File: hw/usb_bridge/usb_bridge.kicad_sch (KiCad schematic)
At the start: 57 parts, among them J1 USB_C_Receptacle_USB2.0_14P, J2 DE9, U1 CH340E, U2 MAX485E, U3 CH334R, U4 74LVC2G04, U5 MCP1754S-3302xCB, U6 TJA1051T-3, Y1 HCI XC53G2-12.000-F20LJDT

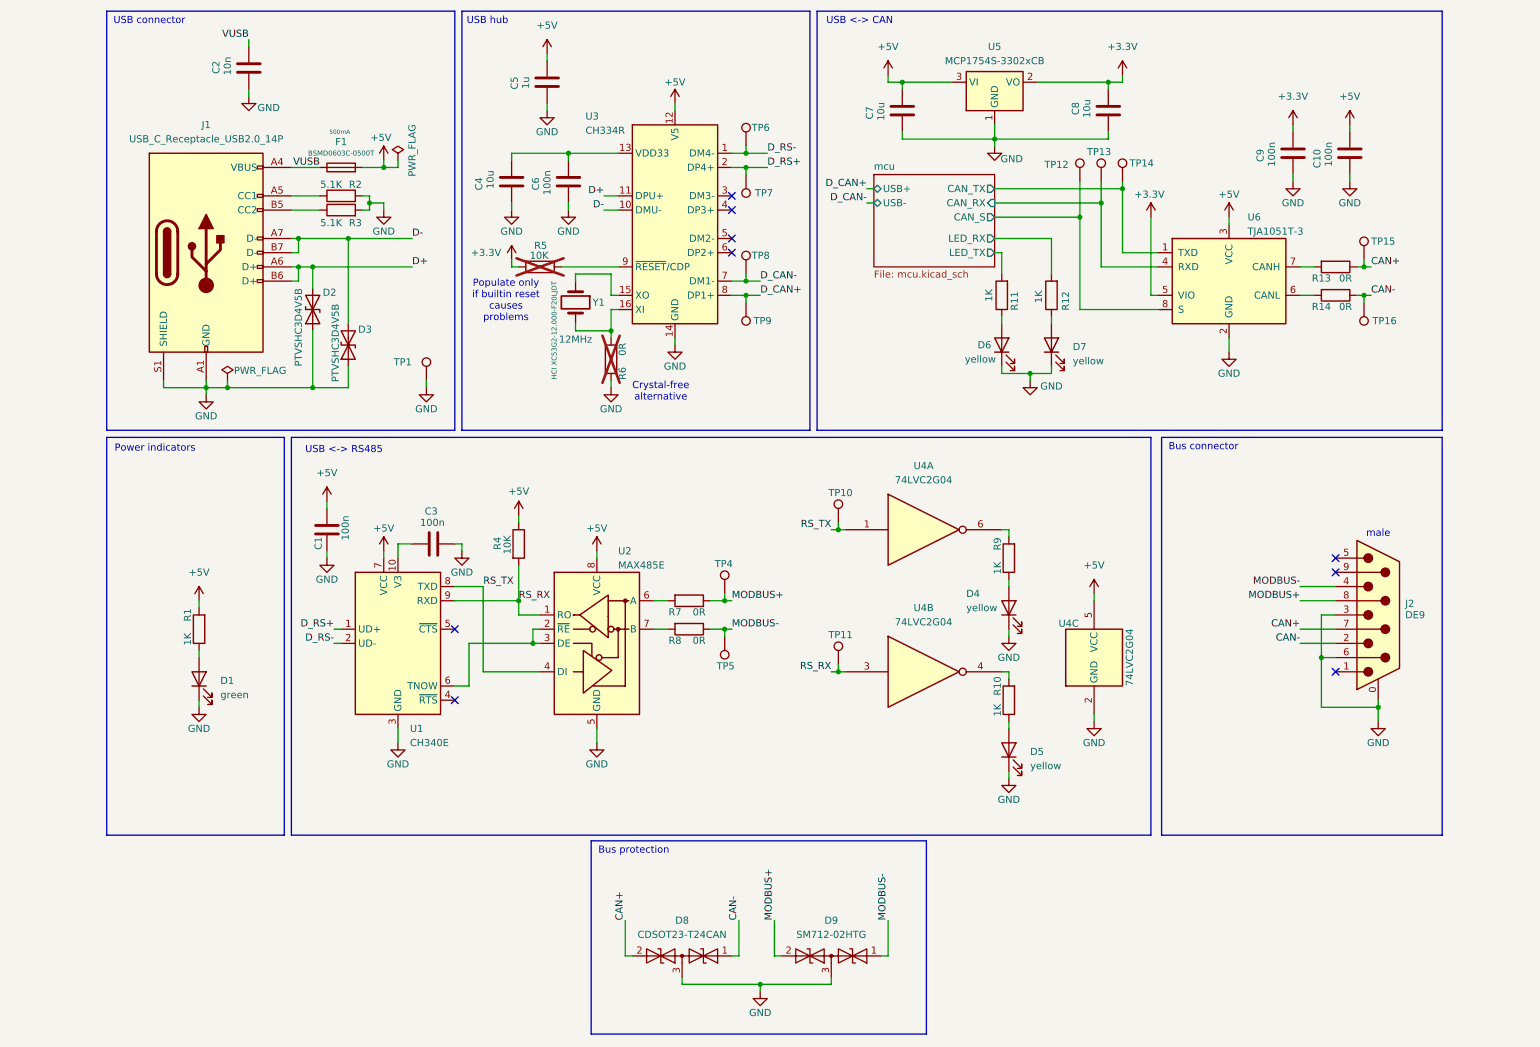
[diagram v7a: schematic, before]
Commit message: Add LED jumper
Signed-off-by: Mateusz Pająk <22417805+Tai-Min@users.noreply.github.com>
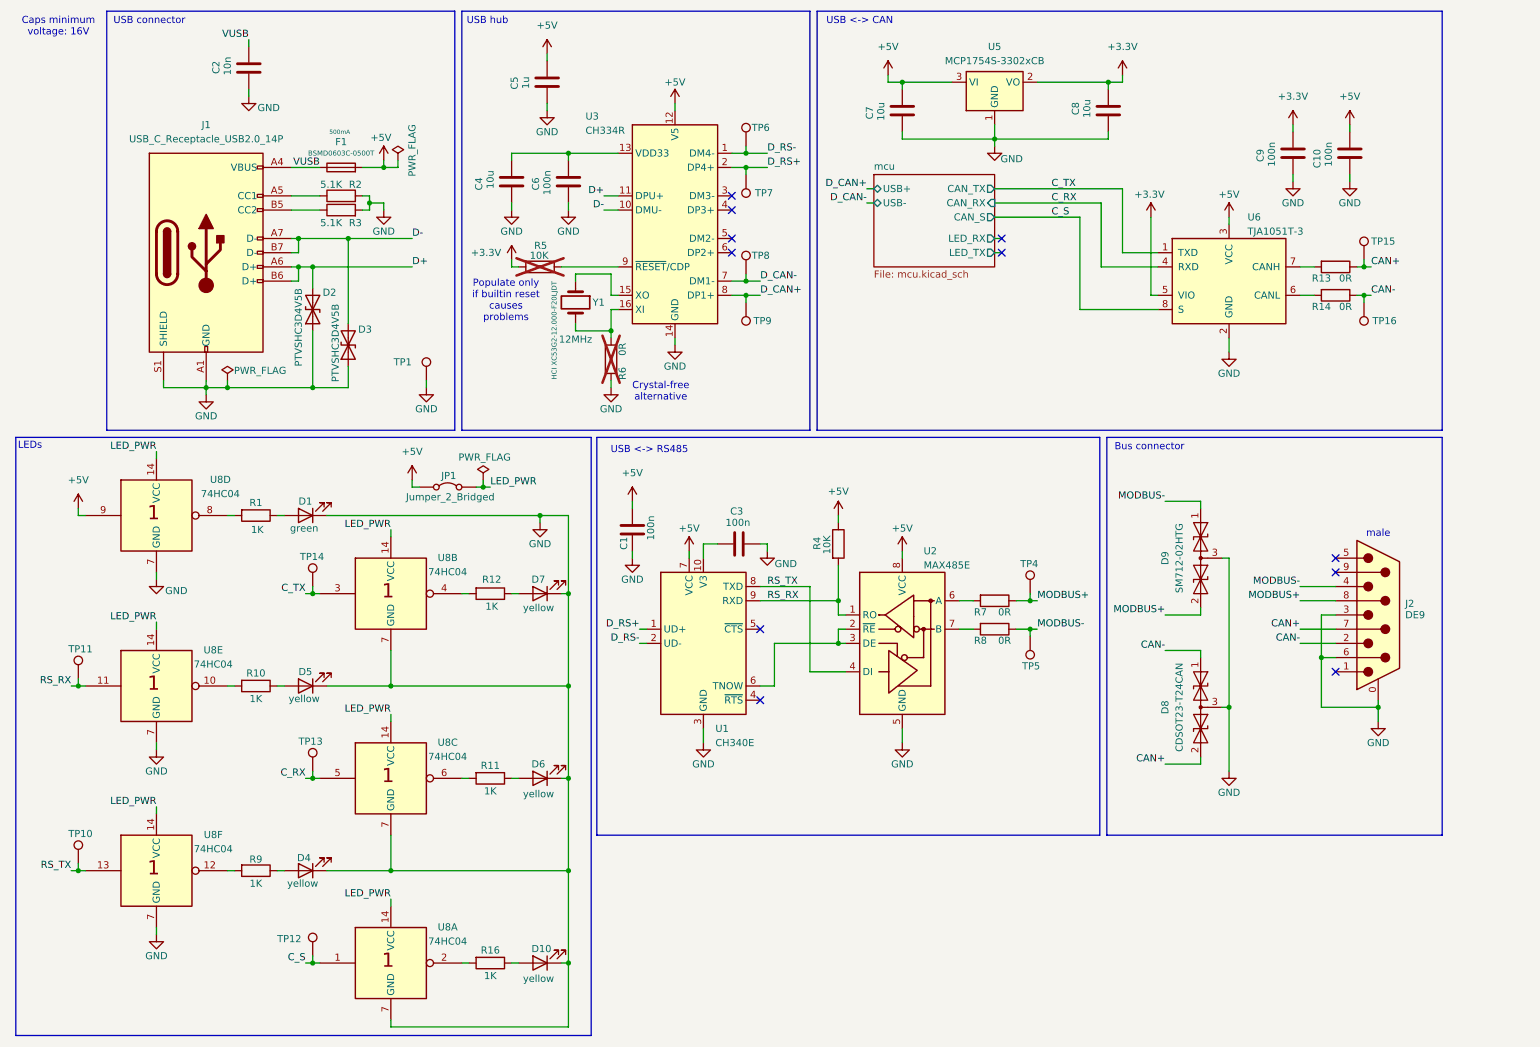
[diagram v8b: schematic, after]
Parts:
- removed U4: 74LVC2G04, Package_TO_SOT_SMD:SOT-23-6, symbol 74xGxx:74LVC2G04
- added D10: yellow, LED_SMD:LED_0603_1608Metric, symbol Device:LED
- added JP1: Jumper_2_Bridged, Jumper:SolderJumper-2_P1.3mm_Bridged_RoundedPad1.0x1.5mm, symbol Jumper:Jumper_2_Bridged
- added R16: 1K, Resistor_SMD:R_0603_1608Metric, symbol Device:R
- added U8: 74HC04, Package_SO:TSSOP-14_4.4x5mm_P0.65mm, symbol 74xx_IEEE:7404
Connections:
- net +5V: now also JP1.1 (A), U8.9; no longer R1.2
- net GND: now also D10.1 (K), U8.7 (GND), U8.7 (GND), U8.7 (GND), U8.7 (GND), U8.7 (GND), U8.7 (GND)
- net RS_RX: now also U8.11
- net RS_TX: now also U8.13
- net mcu/LED_RX: no longer R12.2
- net mcu/LED_TX: no longer R11.2
- net at R9.2: now also U8.12
- net at R10.2: now also U8.10
- net mcu/CAN_RX renamed C_RX
- net C_RX: now also U8.5
- net mcu/CAN_S renamed C_S
- net C_S: now also U8.1
- net mcu/CAN_TX renamed C_TX
- net C_TX: now also U8.3
- new net: R1.2, U8.8
- new net: R12.2, U8.4
- new net: D10.2 (A), R16.1
- new net: R16.2, U8.2
- new net: R11.2, U8.6
- new net LED_PWR: JP1.2 (B), U8.14 (VCC), U8.14 (VCC), U8.14 (VCC), U8.14 (VCC), U8.14 (VCC), U8.14 (VCC)
- no-connect marks 9 -> 11
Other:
- note added: "Caps minimum voltage: 16V"
- note added: "LEDs"
- note removed: "Bus protection"
- note removed: "Power indicators"
- moved on the sheet: C1, C3, D1, D4, D5, D6, D7, D8, D9, R1, R10, R11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
